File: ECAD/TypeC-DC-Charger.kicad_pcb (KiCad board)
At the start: 4 copper layers, 48 x 56 mm, 99 parts, among them CON1 XT60-PT-MALE, J1 USB_C_SOCKET_RA_SMD, Q1 CSD18543Q3A, Q2 CSD18543Q3A, Q3 CSD17551Q3A, Q4 CSD17551Q3A, Q5 CSD17579Q3A, Q6 CSD17579Q3A, Q7 2N7002P, Q8 BC857B, Q9 IRFR9024NTRPBF, SW1 2.54mm_3xSPST_SMD, U1 LM5175RHF, U2 TPS25741, U3 TPS2514

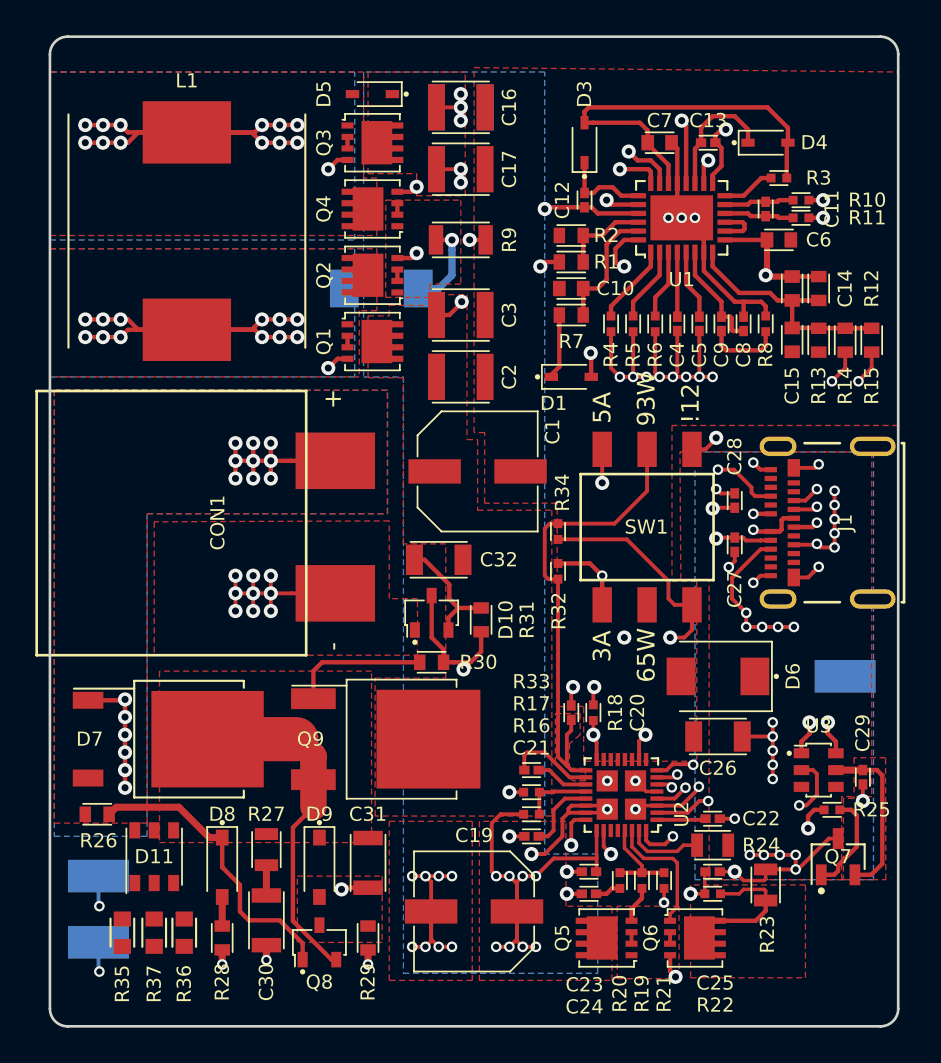
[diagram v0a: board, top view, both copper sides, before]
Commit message: Routing and fixed dip switch disassociated footprint
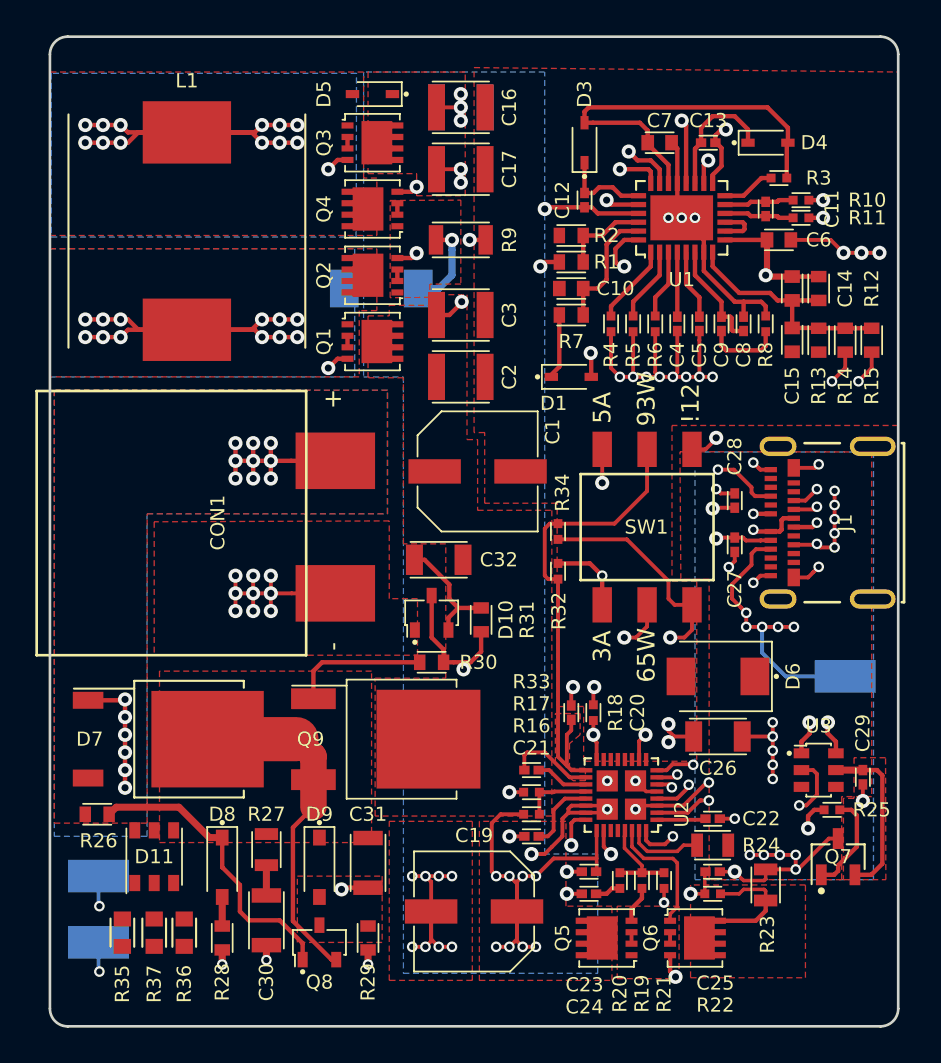
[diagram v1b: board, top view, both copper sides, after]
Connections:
- R35 pad 1: Net-(D11-PadC1) -> Net-(R35-Pad1)
- R36 pad 1: Net-(D11-PadC3) -> Net-(R36-Pad1)
- SW1 pad 3: (no net) -> /USBC Controller/PSEL
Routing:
- net GND: track 118.1 -> 126.5 mm, vias 57 -> 62
- net VBUS: track 45.1 -> 52.0 mm
- net CC1: track 28.0 -> 21.7 mm
- net /USBC Controller/PSEL: track 8.51 -> 11.3 mm

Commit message: RGB led final schematic drawing and prelim resistor selection. Routing and misc board level changes.
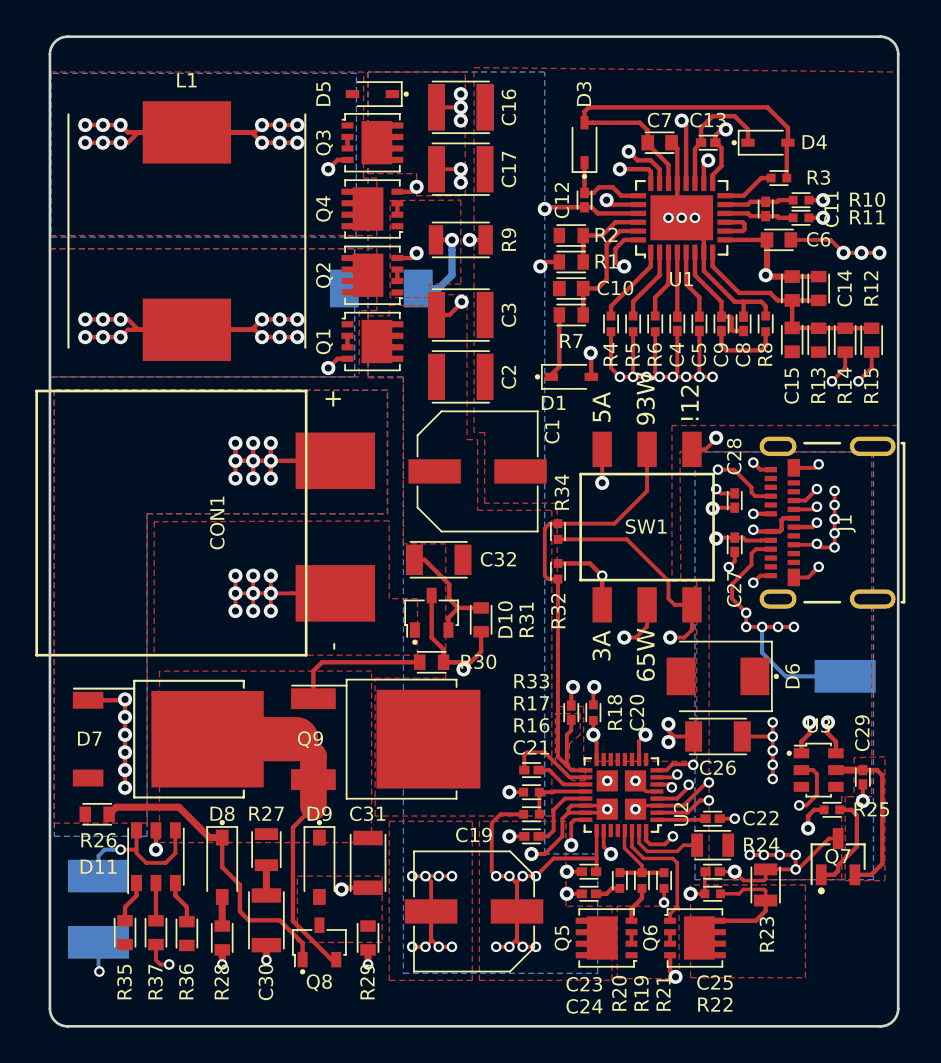
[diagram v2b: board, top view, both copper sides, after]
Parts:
- R35: value 1K00_1608M -> 1K50_1608M; footprint Applidyne_Resistor:RESC1608X50N -> Applidyne_Resistor:RESC1608X50L
- R36: value 1K00_1608M -> 2K40_1608M; footprint Applidyne_Resistor:RESC1608X50N -> Applidyne_Resistor:RESC1608X50L
- R37: value 1K00_1608M -> 330R_1608M; footprint Applidyne_Resistor:RESC1608X50N -> Applidyne_Resistor:RESC1608X50L
- moved R36 0.16 mm to (107.8, 100.8)
- moved R35 0.15 mm to (104.2, 100.7)
- moved D11 0.10 mm to (106.0, 96.4)
- moved R37 0.10 mm to (106.0, 100.7)
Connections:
- C29 pad 1: /Connectors/5V -> 5V
- D11 pad A2: Net-(D11-PadA2) -> 5V
- Q7 pad 2: /Connectors/5V -> 5V
- R35 pad 1: Net-(R35-Pad1) -> Net-(D11-PadC1)
- R36 pad 1: Net-(R36-Pad1) -> Net-(D11-PadC3)
- R37 pad 1: Net-(R37-Pad1) -> Net-(D11-PadC2)
- R37 pad 2: Net-(R37-Pad2) -> GND
- U3 pad 5: /Connectors/5V -> 5V
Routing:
- net 5V: track 0.00 -> 10.6 mm, vias 0 -> 1
- net /Connectors/5V: track 9.56 -> 0.00 mm
- net VARIABLE_DC: track 50.3 -> 57.2 mm
- net Net-(D11-PadC3): track 0.00 -> 2.45 mm
- net Net-(D11-PadC1): track 0.00 -> 2.40 mm
- net Net-(D11-PadC2): track 0.00 -> 2.14 mm
- net GND: track 126.5 -> 128.2 mm, vias 62 -> 63
- net CC2: track 29.1 -> 27.6 mm

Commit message: Routing and cosmetics
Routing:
- net GND: track 128.2 -> 143.3 mm, vias 63 -> 67
- net VARIABLE_DC: track 57.2 -> 59.8 mm, vias 16 -> 19
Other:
- board text added: "GND"
- board text added: "INPUT 9-30VDC 5/12/20V USBC PD2.0 USB2 BC1.2"
- board text added: "REG"
- board text added: "VBUS"

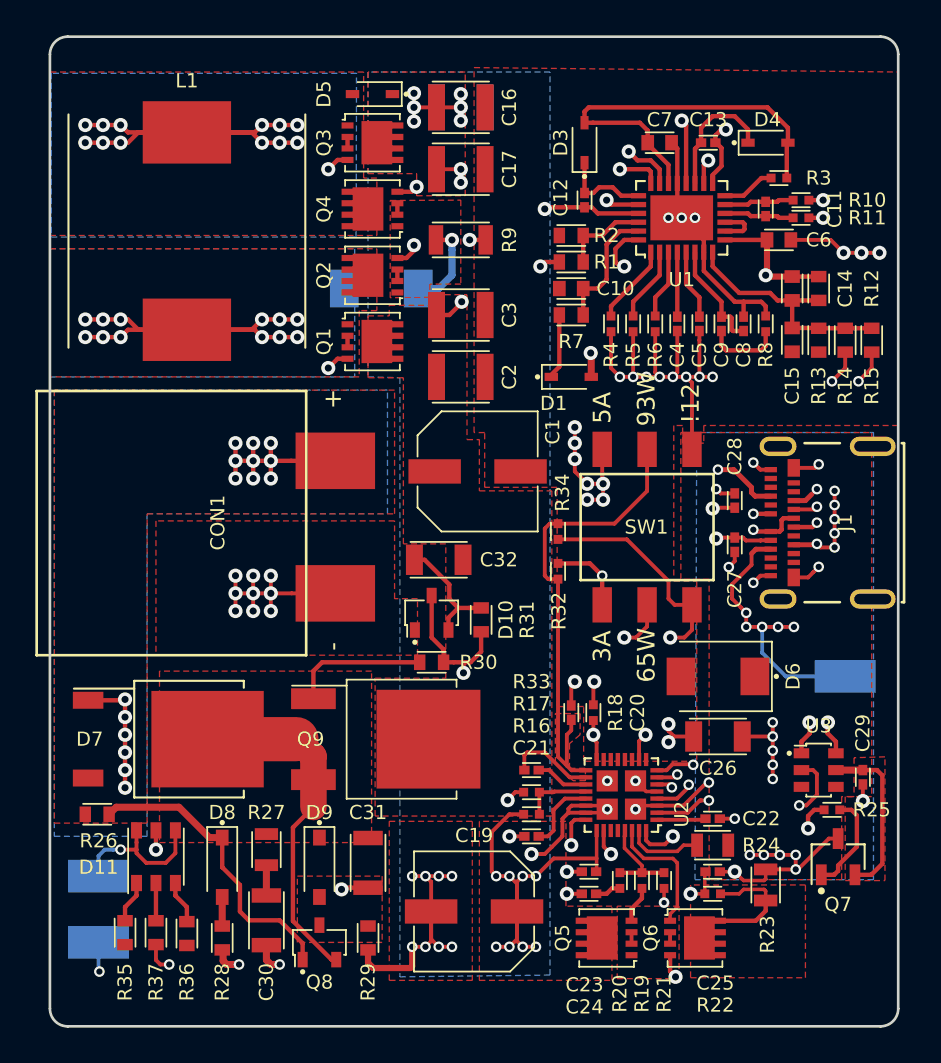
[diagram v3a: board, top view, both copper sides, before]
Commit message: Routing improvements. Silkscreen text and dimensions added. General review of placement and fixes as found.
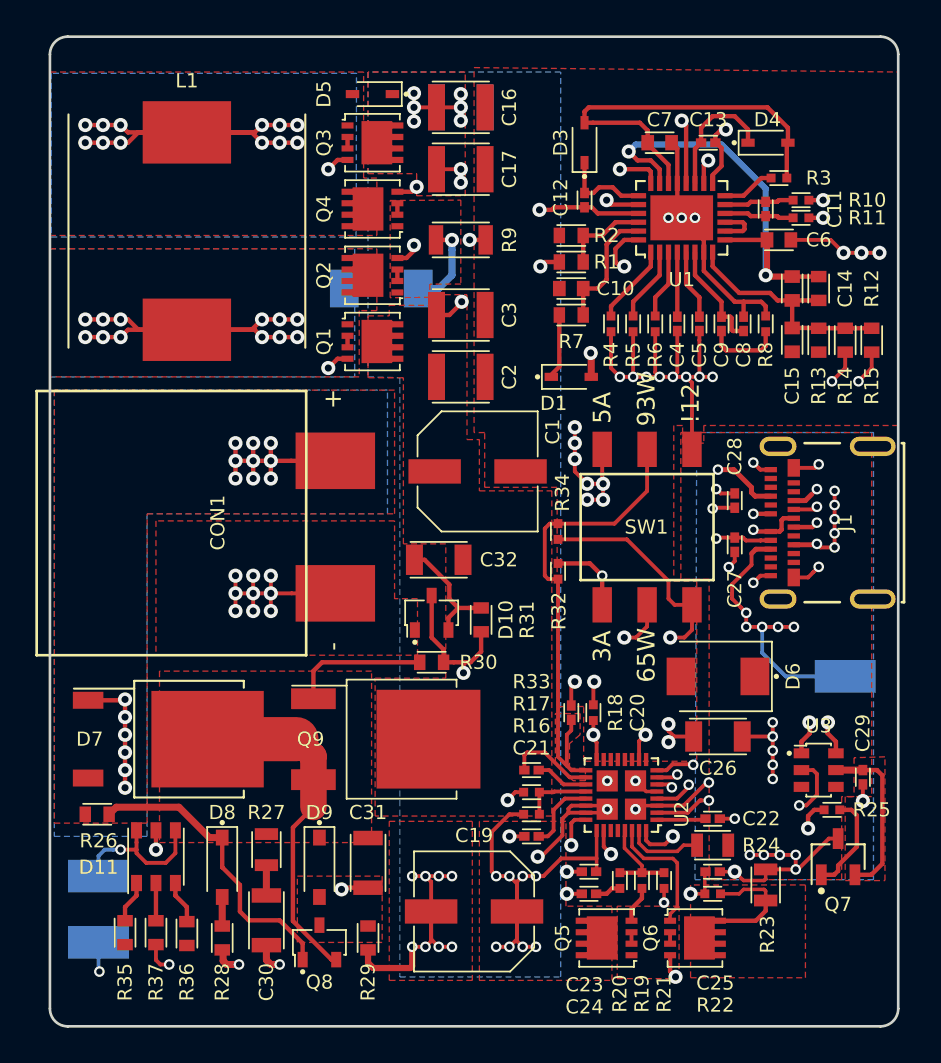
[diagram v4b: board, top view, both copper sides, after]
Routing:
- net VARIABLE_DC: track 59.8 -> 73.7 mm
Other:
- board text added: "4 Layer, 1.0mm thick 70um (2oz) outer layers 17um (0.5oz) inner layers ENIG surface finish Green Soldermask White Silkscreen Min via 0.35mm Min Track: 0.2mm Min clearance: 0.2mm"
- board text added: "SCOTT RAPSON JUNE 2017"

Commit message: Planes, improving pours and routing. Obsessing over small details.
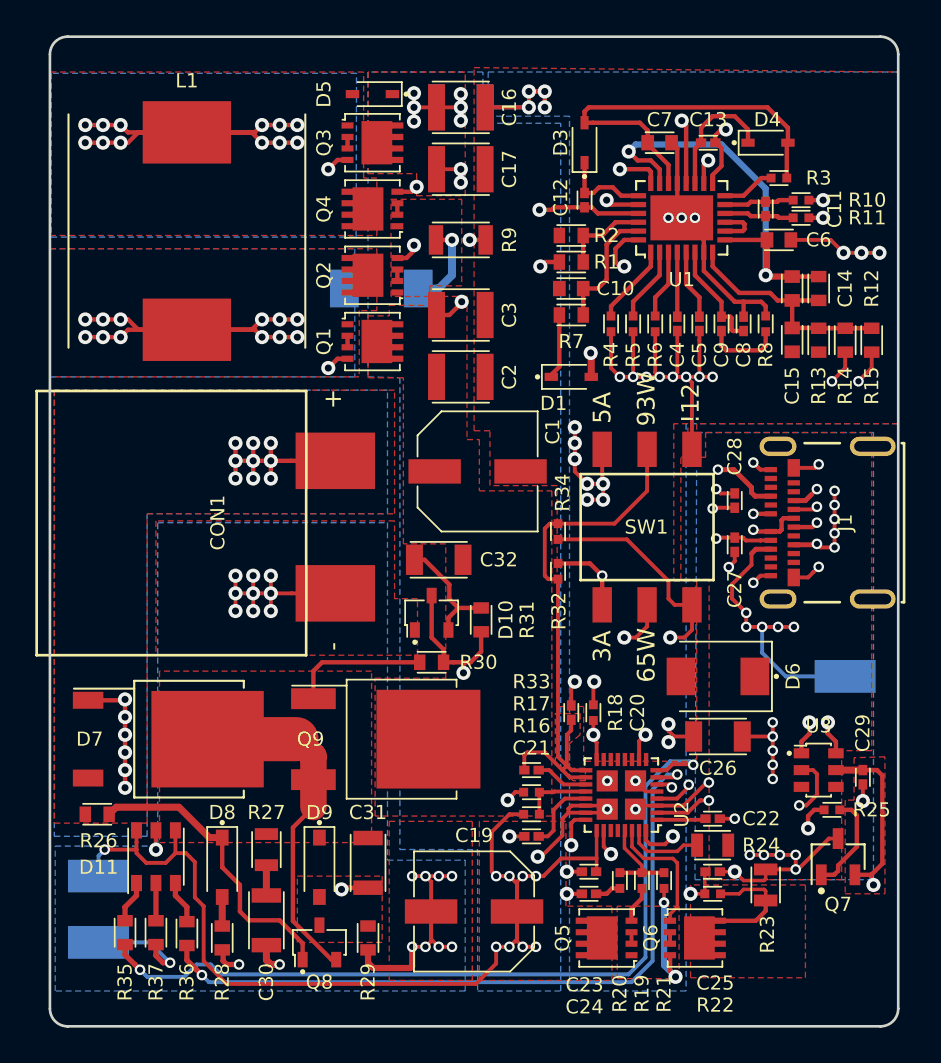
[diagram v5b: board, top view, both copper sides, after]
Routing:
- net 5V: track 10.6 -> 56.7 mm, vias 1 -> 2
- net CTRL2: track 33.8 -> 78.4 mm, vias 2 -> 3
- net CTRL1: track 32.7 -> 72.4 mm, vias 2 -> 3
- net VARIABLE_DC: track 73.7 -> 99.3 mm
- net GND: track 143.0 -> 155.0 mm, vias 67 -> 70
- added copper zone on F.Cu, net 5V
- added copper zone on B.Cu, net GND
- removed copper zone on F.Cu, net /Connectors/5V

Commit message: Finishing touches for pcb
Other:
- board text added: "USBC PD CHARGER SETTINGS"
